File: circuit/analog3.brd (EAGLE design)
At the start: 56.2 x 50.8 mm, 67 parts, among them IC1 OP07C, IC2 74HC4052D, IC3 AD8603UJ, IC4 AD8221R, IC5 AD8221R, IC6 AD8532ARZ

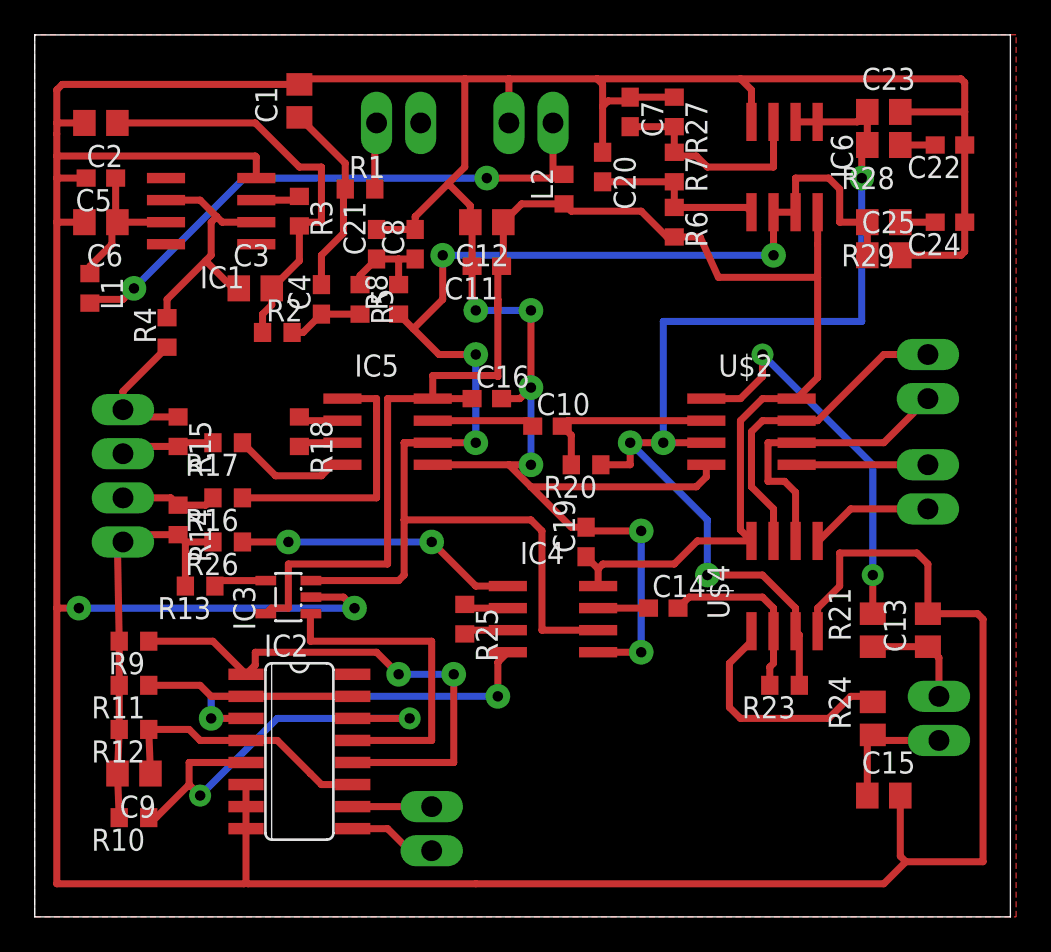
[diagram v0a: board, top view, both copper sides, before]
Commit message: - добавили делитель на генератор
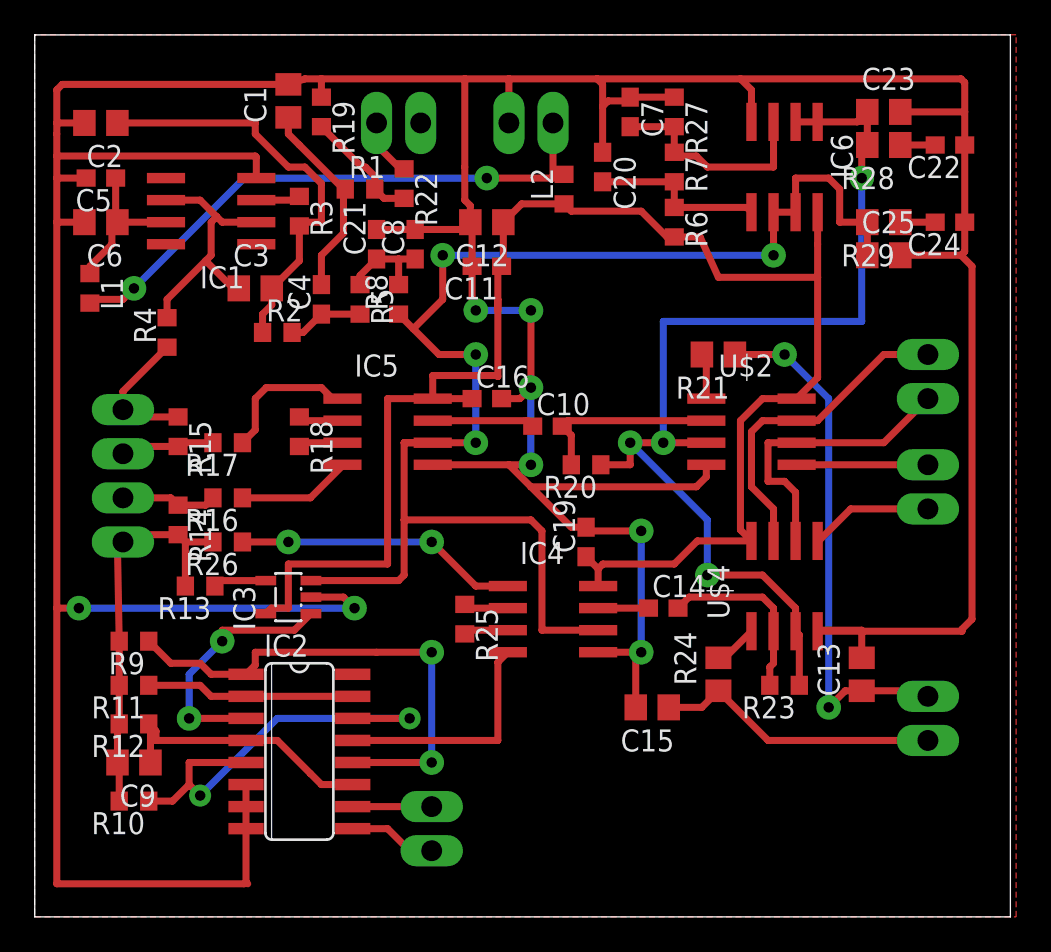
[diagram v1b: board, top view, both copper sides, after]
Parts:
- added R19: 3k, rcl:R0603
- added R22: 12k, rcl:R0603
- moved R21 18.2 mm to (39.4, 32.4), turned to 180 degrees
- moved C15 14.3 mm to (35.6, 12.1), turned to 180 degrees
- moved R24 9.25 mm to (39.4, 14.0)
- moved C13 4.58 mm to (47.6, 14.0)
- moved R10 0.95 mm to (5.71, 6.67)
- moved C1 0.63 mm to (14.6, 47.0)
- moved C9 0.63 mm to (5.71, 8.89)
- moved X5 0.63 mm to (51.4, 11.4)
- moved R12 0.32 mm to (5.71, 11.1)
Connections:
- removed net V_IN+: IC5.1, R16.1
- new net N$32: IC5.4, R16.1
- new net N$34: R1.2, R19.2, R22.2
- net GENERATOR: now also R22.1; no longer R1.2
- net GNDA: now also R19.1
- net N$1: now also IC5.1; no longer IC5.4
- net N$11: now also IC2.3; no longer IC2.13
- net N$30: now also IC2.13; no longer IC2.3
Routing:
- net GNDA: track 330.5 -> 291.2 mm
- net V_ADC: track 6.30 -> 30.5 mm, vias 0 -> 2
- net N$28: track 22.6 -> 2.65 mm, vias 2 -> 0
- net V_IN+: track 15.4 -> 0.00 mm
- net N$26: track 14.1 -> 2.54 mm
- net I_ADC: track 7.57 -> 16.5 mm
- net N$30: track 22.6 -> 13.7 mm, vias 2 -> 0
- net N$34: track 0.00 -> 6.90 mm
- net N$32: track 0.00 -> 6.58 mm
- net N$11: track 18.8 -> 14.7 mm, vias 0 -> 2
- net N$12: track 30.7 -> 28.9 mm
- net N$1: track 6.81 -> 8.39 mm
- net N$18: track 24.1 -> 23.2 mm

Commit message: - убрали лишний конденсатор
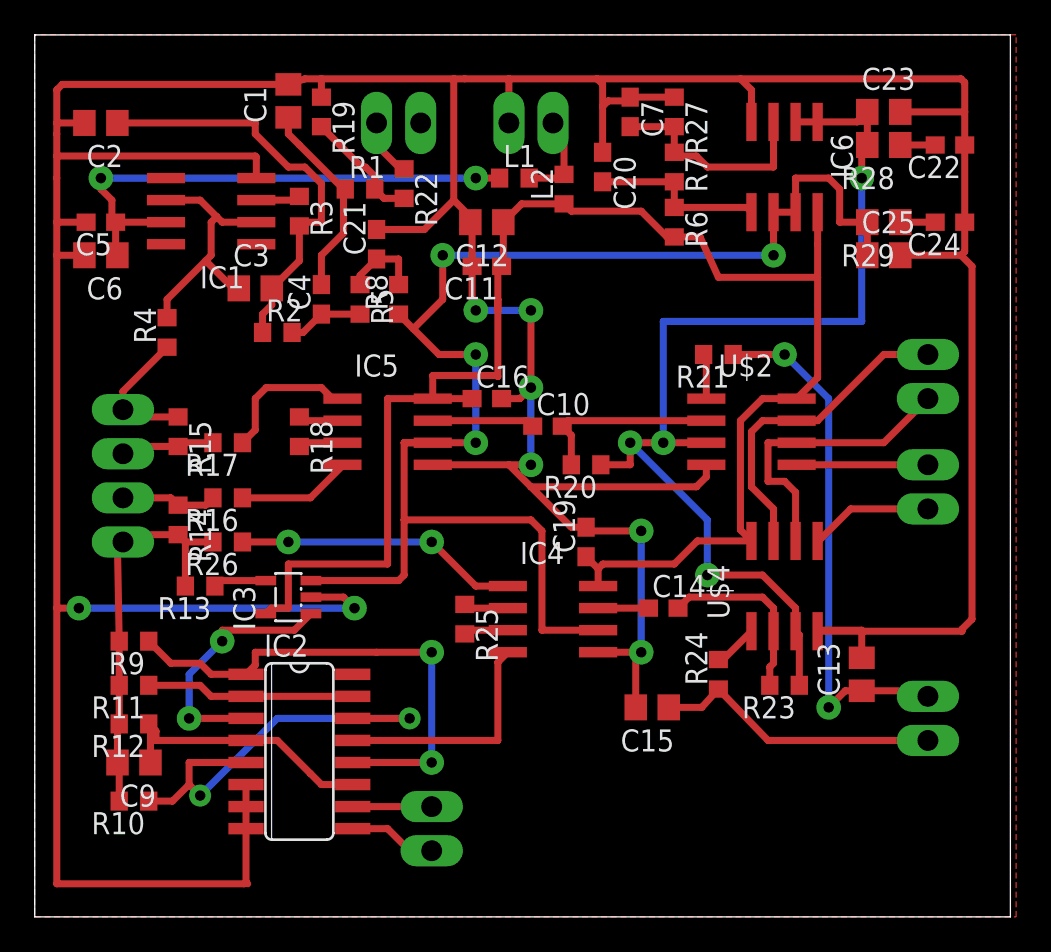
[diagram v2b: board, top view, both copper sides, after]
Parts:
- removed C8: 100n, rcl:C0603
- R18, R25: value 47k -> 27k
- R21, R24: value 1k -> 1.2k; device rcl:R0805 -> rcl:R0603
- moved L1 25.3 mm to (27.6, 42.5), turned to 0 degrees
- moved C5 2.54 mm to (3.81, 40.0)
- moved C6 1.91 mm to (3.81, 38.1)
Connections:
- net GNDA: no longer C8.2
- net N$10: no longer C8.1
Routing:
- net +5V: track 32.8 -> 5.32 mm, vias 2 -> 0
- net N$7: track 9.00 -> 30.7 mm, vias 0 -> 2
- net N$10: track 5.57 -> 4.61 mm

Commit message: - первый вариант разводки под два LM258 в качестве опорного напряжения
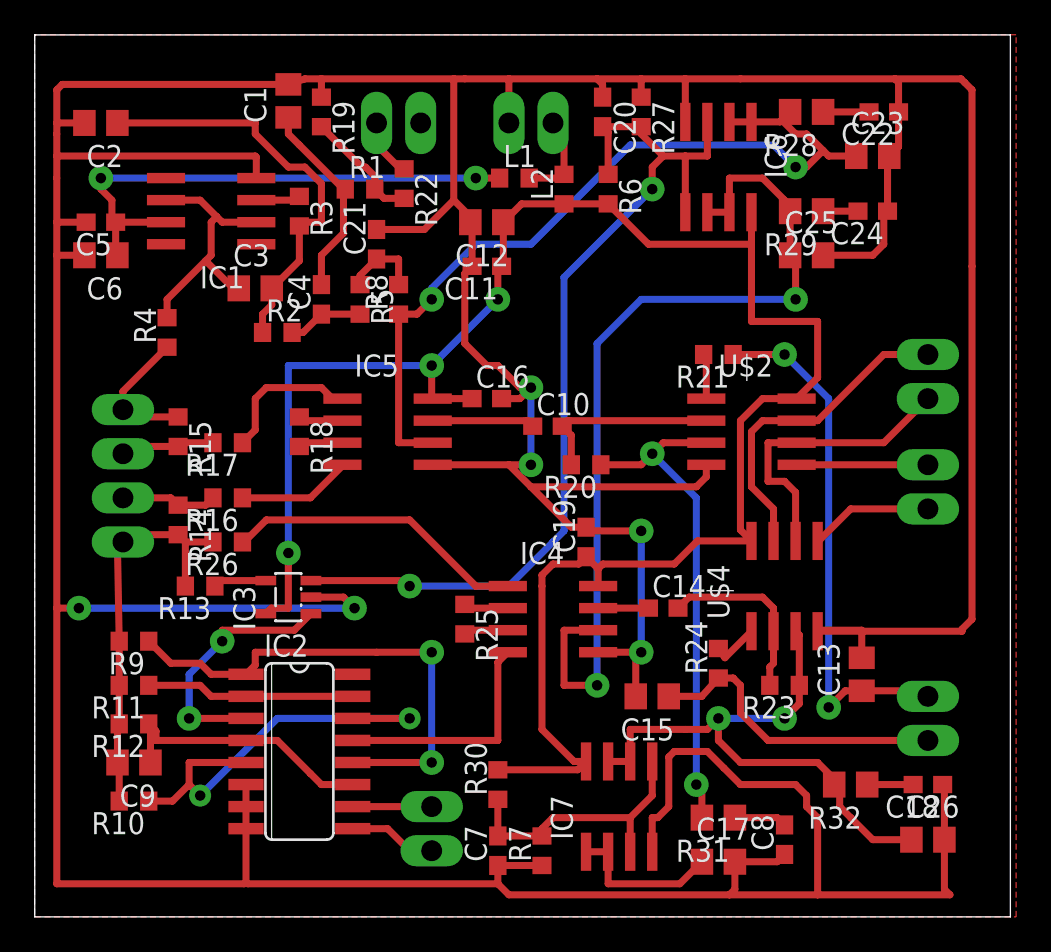
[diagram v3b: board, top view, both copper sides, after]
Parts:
- added C17, C26: 47n, rcl:C0805
- added C18, C8: 1mk, rcl:C0603
- added IC7: LM258, linear:SO08
- added R30: 100k, rcl:R0603
- added R31, R32: 5, rcl:R0805
- IC6: value AD8532ARZ -> LM258
- R27: value 68k -> 100k
- R7: value 39k -> 47k
- moved C7 43.2 mm to (26.7, 3.81), turned to 90 degrees
- moved R7 40.1 mm to (29.2, 3.81), turned to 90 degrees
- moved R28 4.84 mm to (44.5, 46.4)
- moved C24 4.49 mm to (48.3, 40.6)
- moved R29 4.49 mm to (44.5, 40.6)
- moved C25 4.45 mm to (44.5, 38.1)
- moved C22 4.26 mm to (48.9, 46.4)
- moved R6 4.26 mm to (33.0, 41.9)
- moved IC6 3.81 mm to (39.4, 43.2)
- moved C20 3.17 mm to (32.7, 46.4)
- moved C23 2.62 mm to (48.3, 43.8)
- moved R27 1.91 mm to (34.9, 46.4)
- moved C15 0.63 mm to (35.6, 12.7)
- moved R24 0.63 mm to (39.4, 14.6)
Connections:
- removed net +1.6V: C23.1, IC6.1, IC6.2, R20.1, R23.1, R28.2, U$2.3, U$4.3
- removed net +2.5V: C25.1, IC3.3, IC4.6, IC5.6, IC6.6, IC6.7, R29.2, R8.1
- removed net X+2.5V: C20.2, IC6.5, R6.1, R7.2
- new net +1.6V1: C17.1, IC7.1, IC7.2, R20.1, R31.2, U$2.3
- new net +1.6V2: C26.1, IC7.6, IC7.7, R23.1, R32.2, U$4.3
- new net +2.5V0: C20.2, IC3.3, IC6.3, IC6.5, R27.2, R6.1
- new net +2.5V1: C23.1, IC5.6, IC6.1, IC6.2, R28.2, R8.1
- new net +2.5V2: C25.1, IC4.6, IC6.6, IC6.7, R29.2
- new net N$35: C18.2, R32.1
- new net N$41: C7.2, IC7.3, IC7.5, R30.1, R7.2
- net GNDA: now also C17.2, C18.1, C26.2, C8.1, IC7.4, R7.1
- net N$33: now also C8.2, R31.1; no longer C7.2, IC6.3, R27.2, R7.1
- net V+: now also IC7.8, R30.2
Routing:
- net +2.5V: track 84.4 -> 0.00 mm, vias 4 -> 0
- net GNDA: track 291.7 -> 366.9 mm, vias 8 -> 6
- net +1.6V: track 62.2 -> 0.00 mm, vias 4 -> 0
- net +2.5V0: track 0.00 -> 55.0 mm, vias 0 -> 2
- net +2.5V2: track 0.00 -> 52.1 mm, vias 0 -> 2
- net +2.5V1: track 0.00 -> 48.0 mm, vias 0 -> 2
- net +1.6V1: track 0.00 -> 37.8 mm, vias 0 -> 2
- net +1.6V2: track 0.00 -> 33.2 mm, vias 0 -> 2
- net V+: track 93.3 -> 111.4 mm, vias 0 -> 3
- net N$41: track 0.00 -> 16.1 mm
- net X+2.5V: track 10.2 -> 0.00 mm
- net N$33: track 12.7 -> 3.03 mm
- net N$35: track 0.00 -> 2.65 mm
- net I_ADC: track 16.6 -> 17.8 mm
- net N$22: track 16.3 -> 17.4 mm, vias 2 -> 0
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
